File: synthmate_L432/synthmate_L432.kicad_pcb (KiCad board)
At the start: 4 copper layers, 74 x 30 mm, 43 parts, among them J1 USB_C_synthmate, J3 USB_C_connector_board, J5 Conn_01x16, J6 Conn_01x13, J7 Conn_01x04, J8 Conn_ST_STDC14, SW1 RotaryEncoder_Switch, SW2 SW_Push, SW3 SW_Push, U1 STM32L432KCUx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

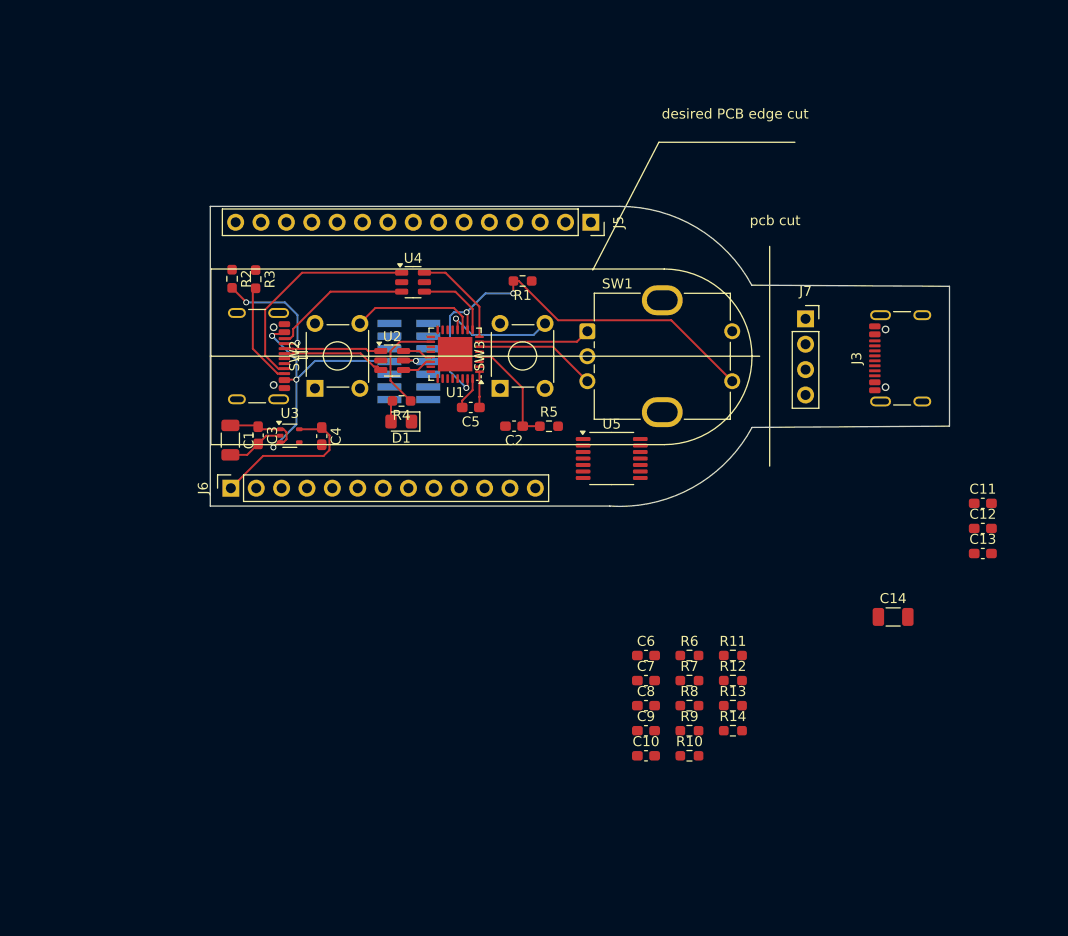
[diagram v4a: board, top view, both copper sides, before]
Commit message: 74LV14 / TPD4E02B04DQA
changed schmitt to 74LV14 and ESD to TPD4E02B04DQA
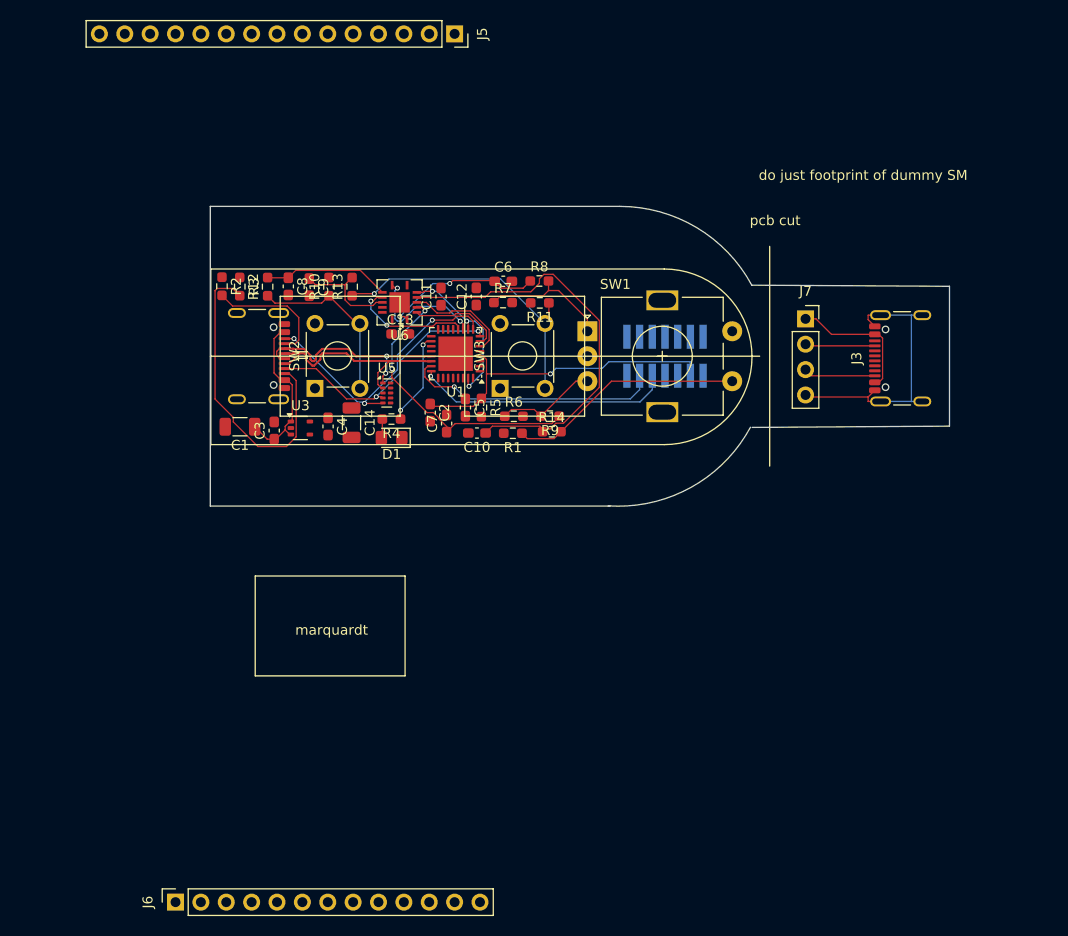
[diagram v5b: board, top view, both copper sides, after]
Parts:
- removed U2, U4: USBLC6-2SC6, Package_TO_SOT_SMD:SOT-23-6
- added U6: 74LV14, Package_DFN_QFN:Texas_S-PVQFN-N14, F.Cu at (110.0, 41.6)
- SW1: footprint Rotary_Encoder:RotaryEncoder_Bourns_Vertical_PEC12R-3x17F-Sxxxx -> Rotary_Encoder:RotaryEncoder_Alps_EC11E-Switch_Vertical_H20mm
- U5: value 40106 -> TPD4E02B04DQA; footprint Package_SO:TSSOP-14_4.4x5mm_P0.65mm -> Package_SON:USON-10_2.5x1.0mm_P0.5mm
- moved C13 62.3 mm to (110.0, 44.8)
- moved R12 61.0 mm to (96.7, 40.0), turned to 90 degrees
- moved R10 59.2 mm to (102.9, 40.0), turned to 90 degrees
- moved C11 58.1 mm to (114.1, 41.0), turned to 90 degrees
- moved C14 57.6 mm to (105.1, 53.7), turned to -90 degrees
- moved R13 56.7 mm to (105.2, 40.0), turned to 90 degrees
- moved C12 55.8 mm to (117.6, 41.0), turned to 90 degrees
- moved C9 55.7 mm to (100.9, 40.1), turned to -90 degrees
- moved C8 55.2 mm to (98.8, 40.0), turned to -90 degrees
- moved R8 45.1 mm to (123.9, 39.5)
- moved R7 42.2 mm to (120.3, 41.6)
- moved J6 41.8 mm to (87.5, 101.7)
- moved R11 40.2 mm to (124.0, 41.7), turned to 180 degrees
- moved C6 40.1 mm to (120.3, 39.5)
- moved C10 36.5 mm to (117.7, 54.7), turned to 180 degrees
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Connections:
- J1 pad A6: /usb_P -> /usb+
- J1 pad A7: /usb_N -> /usb-
- J1 pad A8: Net-(J1-SBU1) -> LPUART_TX
- J1 pad B6: /usb_P -> /usb+
- J1 pad B7: /usb_N -> /usb-
- J1 pad B8: Net-(J1-SBU2) -> LPUART_RX
- J8 pad 12: unconnected-(J8-~{RST}-Pad12) -> NRST
- J8 pad 3: unconnected-(J8-VCC-Pad3) -> 3V3
- J8 pad 4: unconnected-(J8-JTMS/SWDIO-Pad4) -> SWDIO
- J8 pad 5: Net-(J8-GND-Pad5) -> GND
- J8 pad 6: unconnected-(J8-JCLK/SWCLK-Pad6) -> SWCLK
- J8 pad 7: Net-(J8-GND-Pad5) -> GND
- U1 pad 23: PA13 -> SWDIO
- U1 pad 24: PA14 -> SWCLK
- U5 pad 1: Net-(C6-Pad1) -> /usb-
- U5 pad 10: pushbutton_B -> unconnected-(U5-NC-Pad10)
- U5 pad 2: enc_A -> /usb+
- U5 pad 3: Net-(C7-Pad1) -> GND
- U5 pad 4: enc_B -> LPUART_TX
- U5 pad 5: Net-(C10-Pad1) -> LPUART_RX
- U5 pad 6: BOOT0 -> unconnected-(U5-NC-Pad6)
- U5 pad 7: GND -> unconnected-(U5-NC-Pad7)
- U5 pad 8: pushbutton_A -> GND
- U5 pad 9: Net-(C8-Pad1) -> unconnected-(U5-NC-Pad9)
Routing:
- net Net-(C10-Pad1): track 0.00 -> 41.9 mm
- net Net-(R11-Pad1): track 0.00 -> 30.6 mm, vias 0 -> 1
- net Net-(C7-Pad1): track 0.00 -> 29.0 mm, vias 0 -> 2
- net BOOT0: track 45.2 -> 16.3 mm
- net adaptor_GND: track 0.00 -> 28.6 mm
- net SWDIO: track 0.00 -> 25.7 mm, vias 0 -> 1
- net SWCLK: track 0.00 -> 25.7 mm, vias 0 -> 1
- net Net-(R1-Pad1): track 0.00 -> 23.7 mm
- net Net-(J1-SBU1): track 22.3 -> 0.00 mm
- net NRST: track 11.2 -> 32.7 mm, vias 0 -> 1
- net 5V: track 38.0 -> 16.6 mm, vias 4 -> 0
- net LPUART_RX: track 7.63 -> 29.0 mm, vias 0 -> 3
- net Net-(J1-CC2): track 10.4 -> 31.6 mm
- net 3V3: track 19.9 -> 0.00 mm
- net /usb+: track 3.07 -> 22.0 mm
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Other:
- outline, holes or cut-outs redrawn
- board text added: "do just footprint of dummy SM"
- board text added: "marquardt"
- board text removed: "desired PCB edge cut"

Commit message: moved smd to bottom side, changed back to eusblc6
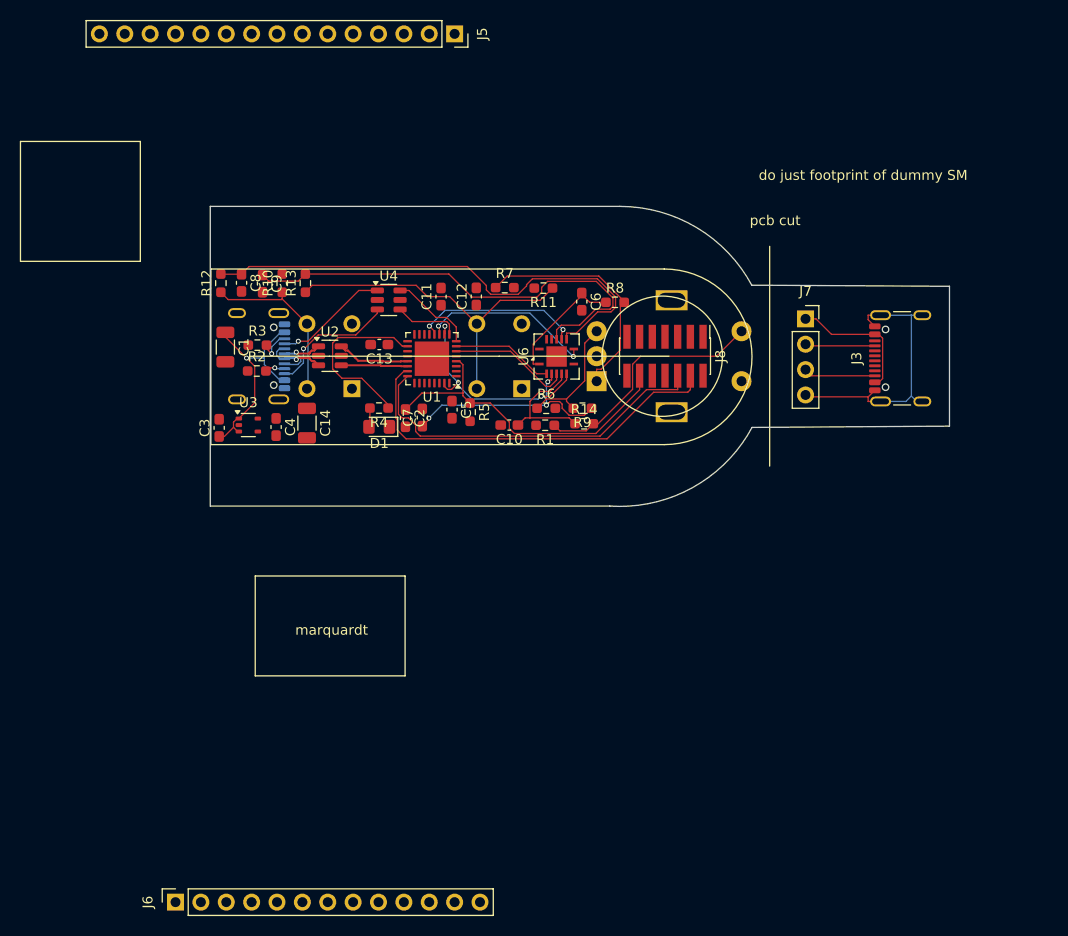
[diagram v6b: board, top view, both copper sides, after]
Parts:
- removed U5: TPD4E02B04DQA, Package_SON:USON-10_2.5x1.0mm_P0.5mm
- added U2: USBLC6-2SC6, Package_TO_SOT_SMD:SOT-23-6, F.Cu at (103.0, 47.0)
- added U4: USBLC6-2SC6, Package_TO_SOT_SMD:SOT-23-6, F.Cu at (108.9, 41.4)
- J1, SW1, SW2, SW3: moved to B.Cu
- J8: moved to F.Cu
- moved U6 16.6 mm to (125.7, 47.0), turned to 90 degrees
- moved R2 9.17 mm to (95.7, 48.5), turned to 0 degrees
- moved C6 8.12 mm to (128.2, 41.5), turned to -90 degrees
- moved C1 8.11 mm to (92.5, 46.1), turned to -90 degrees
- moved R8 7.87 mm to (131.5, 41.6)
- moved R3 6.12 mm to (95.7, 45.9), turned to 0 degrees
- moved C3 5.52 mm to (91.9, 54.2)
- moved U3 5.22 mm to (94.8, 53.9)
- moved C4 5.20 mm to (97.6, 54.1)
- moved SW1 5.09 mm to (129.7, 49.5)
- moved R13 4.69 mm to (100.5, 39.7)
- moved C8 4.69 mm to (94.1, 39.7)
- moved R10 4.69 mm to (98.2, 39.7)
- moved R12 4.69 mm to (92.1, 39.7)
- moved C9 4.69 mm to (96.2, 39.7)
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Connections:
- J1 pad A6: /usb+ -> /usb_P
- J1 pad A7: /usb- -> /usb_N
- J1 pad A8: LPUART_TX -> Net-(J1-SBU1)
- J1 pad B6: /usb+ -> /usb_P
- J1 pad B7: /usb- -> /usb_N
- J1 pad B8: LPUART_RX -> Net-(J1-SBU2)
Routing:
- net Net-(C8-Pad1): track 12.7 -> 50.3 mm
- net Net-(C9-Pad1): track 10.5 -> 46.6 mm
- net Net-(C10-Pad1): track 41.9 -> 12.6 mm
- net Net-(J1-CC2): track 31.6 -> 3.38 mm, vias 0 -> 1
- net LPUART_RX: track 29.0 -> 6.56 mm, vias 3 -> 0
- net LPUART_TX: track 25.5 -> 8.56 mm, vias 2 -> 0
- net /usb+: track 22.0 -> 6.68 mm
- net /usb-: track 21.7 -> 7.28 mm, vias 2 -> 0
- net SWDIO: track 25.7 -> 39.8 mm, vias 1 -> 0
- net Net-(J1-SBU2): track 0.00 -> 13.0 mm, vias 0 -> 1
- net Net-(J1-SBU1): track 0.00 -> 11.5 mm, vias 0 -> 1
- net SWCLK: track 25.7 -> 36.7 mm, vias 1 -> 0
- net Net-(R7-Pad1): track 13.2 -> 23.8 mm
- net Net-(J1-CC1): track 12.5 -> 2.03 mm, vias 0 -> 1
- net LED: track 9.33 -> 18.1 mm, vias 2 -> 0
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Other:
- outline, holes or cut-outs redrawn
